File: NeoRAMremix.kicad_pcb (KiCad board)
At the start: 2 copper layers, 58.2 x 84.1 mm, 28 parts, among them P1 C64-Exp-Port, Q1 2N3904, SW1 Reset, U1 HM628512BFP-5, U2 HM628512BFP-5, U3 HM628512BFP-5, U4 HM628512BFP-5

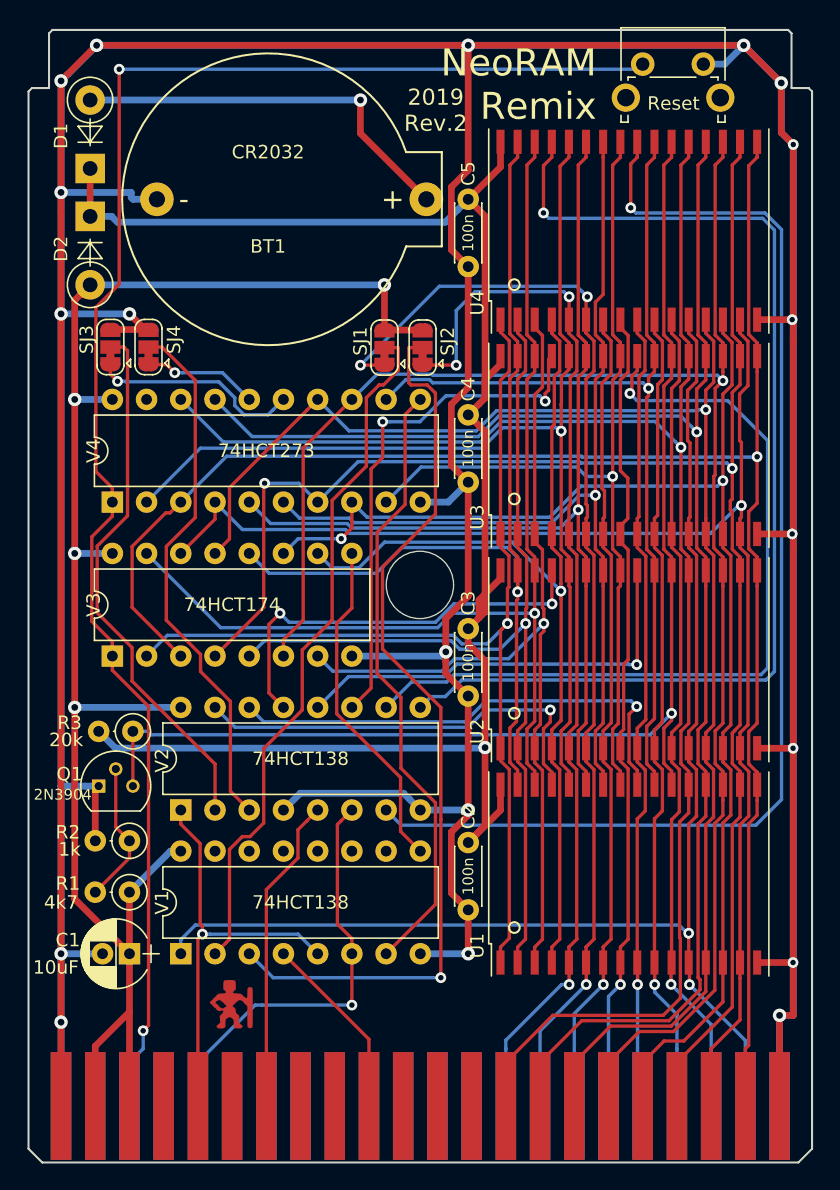
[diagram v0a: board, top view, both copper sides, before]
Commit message: Added JP1 to disable battery circuit for /CS.
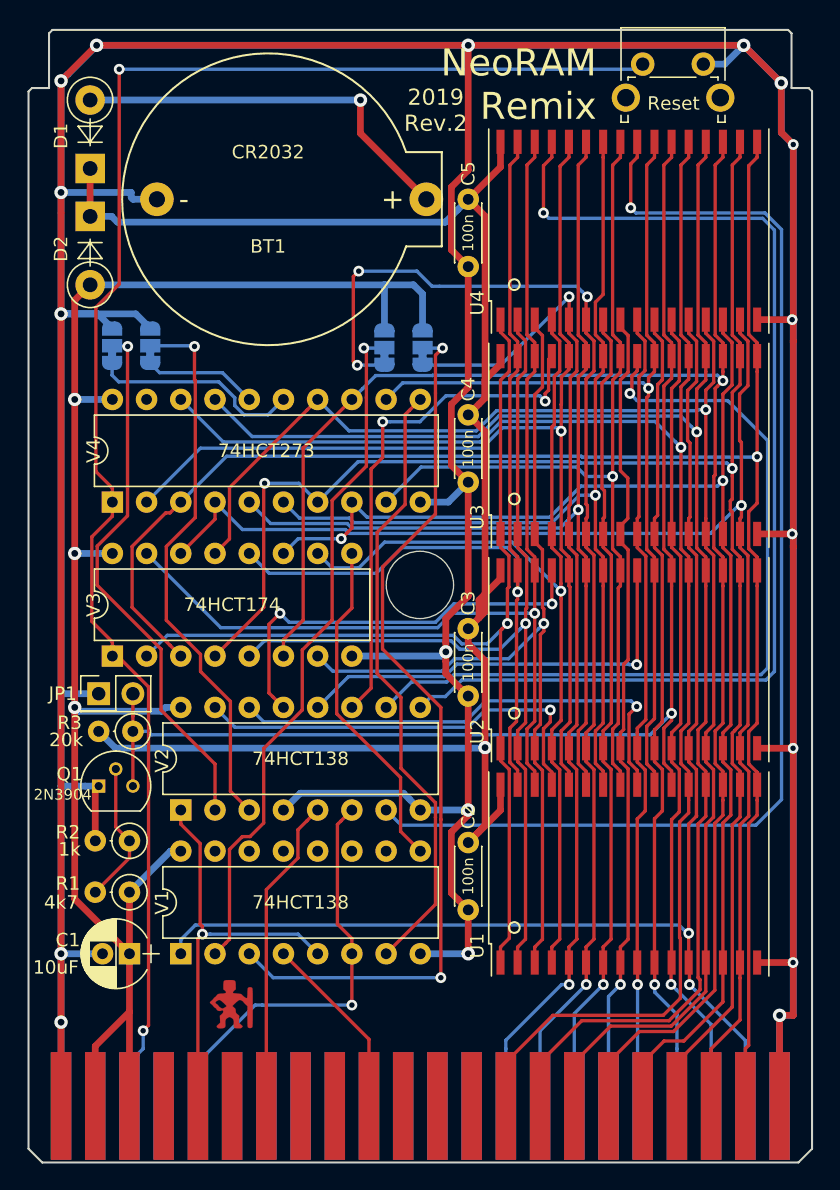
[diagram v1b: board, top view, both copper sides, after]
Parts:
- added JP1: no_battery, Pin_Headers:Pin_Header_Straight_2x01_Pitch2.54mm, F.Cu at (89.2, 100.1)
- SJ1, SJ2, SJ3, SJ4: moved to B.Cu
- moved SJ4 0.16 mm to (93.0, 74.2)
- moved SJ3 0.16 mm to (90.2, 74.2)
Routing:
- net /A6: track 84.5 -> 90.1 mm, vias 3 -> 4
- net GND: track 562.0 -> 566.3 mm, vias 19 -> 18
- net +5V: track 122.3 -> 125.5 mm, vias 4 -> 3
- net Net-(JP1-Pad2): track 94.0 -> 96.8 mm
- net /A7: track 79.5 -> 76.8 mm, vias 3 -> 2
- net Net-(SJ4-Pad2): track 39.8 -> 41.2 mm, vias 0 -> 1
- net Net-(SJ2-Pad2): track 67.7 -> 66.8 mm, vias 1 -> 2
- net Net-(SJ1-Pad2): track 52.2 -> 51.6 mm, vias 0 -> 1
- net Net-(SJ3-Pad2): track 40.0 -> 40.2 mm, vias 0 -> 1
- net Net-(SJ4-Pad1): track 8.55 -> 8.46 mm, vias 1 -> 0
- net Net-(SJ3-Pad1): vias 1 -> 0
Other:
- board text added: "NeoRAM Remix Rev.2 Original design (2007): http://www.x1541.de/ Remix (2019): https://www.hackup.net/"
- board text removed: "NeoRAM Remix Rev.1 Original design (2007): http://www.x1541.de/ Remix (2019): https://www.hackup.net/"

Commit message: Added repo URL.
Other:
- board text added: "NeoRAM Remix Rev.2 https://github.com/hackup/NeoRAMremix Original design (2007): http://www.x1541.de/ Remix (2019): https://www.hackup.net/"
- board text removed: "NeoRAM Remix Rev.2 Original design (2007): http://www.x1541.de/ Remix (2019): https://www.hackup.net/"
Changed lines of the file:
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@@
     )
   )
-  (gr_text "NeoRAM Remix Rev.2\nOriginal design (2007): http://www.x1541.de/\nRemix (2019): https://www.hackup.net/" (at 134.62 120.523 270) (layer B.SilkS)
+  (gr_text "NeoRAM Remix Rev.2\nhttps://github.com/hackup/NeoRAMremix\nOriginal design (2007): http://www.x1541.de/\nRemix (2019): https://www.hackup.net/" (at 134.62 120.523 270) (layer B.SilkS)
     (effects (font (size 1.5 1.5) (thickness 0.3)) (justify left mirror))
   )
@@
   (segment (start 91.44 112.268) (end 91.44 110.998) (width 0.25) (layer F.Cu) (net 26))
   (segment (start 88.9 114.808) (end 91.44 112.268) (width 0.25) (layer F.Cu) (net 26))
-  (segment (start 91.694 106.934) (end 91.694 102.87) (width 0.25) (layer F.Cu) (net 54))
-  (segment (start 131.683001 92.074999) (end 131.683001 90.924999) (width 0.25) (layer F.Cu) (net 54))
-  (segment (start 131.108 102.6297) (end 131.683001 102.054699) (width 0.25) (layer F.Cu) (net 54))
-  (segment (start 131.108 105.245) (end 131.108 102.6297) (width 0.25) (layer F.Cu) (net 54))
-  (segment (start 131.683001 105.820001) (end 131.108 105.245) (width 0.25) (layer F.Cu) (net 54))
-  (segment (start 131.683001 106.832999) (end 131.683001 105.820001) (width 0.25) (layer F.Cu) (net 54))
-  (segment (start 131.683001 76.654699) (end 131.683001 76.166999) (width 0.25) (layer F.Cu) (net 54))
-  (segment (start 131.683001 76.166999) (end 131.683001 75.016999) (width 0.25) (layer F.Cu) (net 54))
-  (segment (start 131.683001 89.934297) (end 131.108 89.359296) (width 0.25) (layer F.Cu) (net 54))
-  (segment (start 131.683001 90.924999) (end 131.683001 89.934297) (width 0.25) (layer F.Cu) (net 54))
-  (segment (start 131.108 77.2297) (end 131.683001 76.654699) (width 0.25) (layer F.Cu) (net 54))
-  (segment (start 131.108 89.359296) (end 131.108 77.2297) (width 0.25) (layer F.Cu) (net 54))
-  (segment (start 131.108 60.834) (end 131.683001 60.258999) (width 0.25) (layer F.Cu) (net 54))
-  (segment (start 131.683001 60.258999) (end 131.683001 59.108999) (width 0.25) (layer F.Cu) (net 54))
-  (segment (start 131.108 73.451296) (end 131.108 60.834) (width 0.25) (layer F.Cu) (net 54))
-  (segment (start 131.683001 75.016999) (end 131.683001 74.026297) (width 0.25) (layer F.Cu) (net 54))
-  (segment (start 131.683001 74.026297) (end 131.108 73.451296) (width 0.25) (layer F.Cu) (net 54))
-  (segment (start 92.82537 102.87) (end 93.07937 103.124) (width 0.25) (layer B.Cu) (net 54))
-  (segment (start 91.694 102.87) (end 92.82537 102.87) (width 0.25) (layer B.Cu) (net 54))
-  (via (at 131.683001 101.5365) (size 0.8) (drill 0.4) (layers F.Cu B.Cu) (net 54))
-  (segment (start 130.095501 103.124) (end 131.683001 101.5365) (width 0.25) (layer B.Cu) (net 54))
-  (segment (start 93.07937 103.124) (end 130.095501 103.124) (width 0.25) (layer B.Cu) (net 54))
-  (segment (start 131.683001 101.5365) (end 131.683001 92.074999) (width 0.25) (layer F.Cu) (net 54))
-  (segment (start 131.683001 102.054699) (end 131.683001 101.5365) (width 0.25) (layer F.Cu) (net 54))
   (segment (start 90.150005 76.434005) (end 90.150005 75.547036) (width 0.25) (layer B.Cu) (net 27))
   (segment (start 90.63827 76.92227) (end 90.150005 76.434005) (width 0.25) (layer B.Cu) (net 27))
@@
   (segment (start 96.266 76.755959) (end 96.325001 76.81496) (width 0.25) (layer F.Cu) (net 53))
   (segment (start 96.266 74.295) (end 96.266 76.755959) (width 0.25) (layer F.Cu) (net 53))
+  (segment (start 91.694 106.934) (end 91.694 102.87) (width 0.25) (layer F.Cu) (net 54))
+  (segment (start 131.683001 92.074999) (end 131.683001 90.924999) (width 0.25) (layer F.Cu) (net 54))
+  (segment (start 131.108 102.6297) (end 131.683001 102.054699) (width 0.25) (layer F.Cu) (net 54))
+  (segment (start 131.108 105.245) (end 131.108 102.6297) (width 0.25) (layer F.Cu) (net 54))
+  (segment (start 131.683001 105.820001) (end 131.108 105.245) (width 0.25) (layer F.Cu) (net 54))
+  (segment (start 131.683001 106.832999) (end 131.683001 105.820001) (width 0.25) (layer F.Cu) (net 54))
+  (segment (start 131.683001 76.654699) (end 131.683001 76.166999) (width 0.25) (layer F.Cu) (net 54))
+  (segment (start 131.683001 76.166999) (end 131.683001 75.016999) (width 0.25) (layer F.Cu) (net 54))
+  (segment (start 131.683001 89.934297) (end 131.108 89.359296) (width 0.25) (layer F.Cu) (net 54))
+  (segment (start 131.683001 90.924999) (end 131.683001 89.934297) (width 0.25) (layer F.Cu) (net 54))
+  (segment (start 131.108 77.2297) (end 131.683001 76.654699) (width 0.25) (layer F.Cu) (net 54))
+  (segment (start 131.108 89.359296) (end 131.108 77.2297) (width 0.25) (layer F.Cu) (net 54))
+  (segment (start 131.108 60.834) (end 131.683001 60.258999) (width 0.25) (layer F.Cu) (net 54))
+  (segment (start 131.683001 60.258999) (end 131.683001 59.108999) (width 0.25) (layer F.Cu) (net 54))
+  (segment (start 131.108 73.451296) (end 131.108 60.834) (width 0.25) (layer F.Cu) (net 54))
+  (segment (start 131.683001 75.016999) (end 131.683001 74.026297) (width 0.25) (layer F.Cu) (net 54))
+  (segment (start 131.683001 74.026297) (end 131.108 73.451296) (width 0.25) (layer F.Cu) (net 54))
+  (segment (start 92.82537 102.87) (end 93.07937 103.124) (width 0.25) (layer B.Cu) (net 54))
+  (segment (start 91.694 102.87) (end 92.82537 102.87) (width 0.25) (layer B.Cu) (net 54))
+  (via (at 131.683001 101.5365) (size 0.8) (drill 0.4) (layers F.Cu B.Cu) (net 54))
+  (segment (start 130.095501 103.124) (end 131.683001 101.5365) (width 0.25) (layer B.Cu) (net 54))
+  (segment (start 93.07937 103.124) (end 130.095501 103.124) (width 0.25) (layer B.Cu) (net 54))
+  (segment (start 131.683001 101.5365) (end 131.683001 92.074999) (width 0.25) (layer F.Cu) (net 54))
+  (segment (start 131.683001 102.054699) (end 131.683001 101.5365) (width 0.25) (layer F.Cu) (net 54))
   (segment (start 91.694 101.73863) (end 91.694 100.076) (width 0.25) (layer F.Cu) (net 54))
   (segment (start 91.694 102.87) (end 91.694 101.73863) (width 0.25) (layer F.Cu) (net 54))

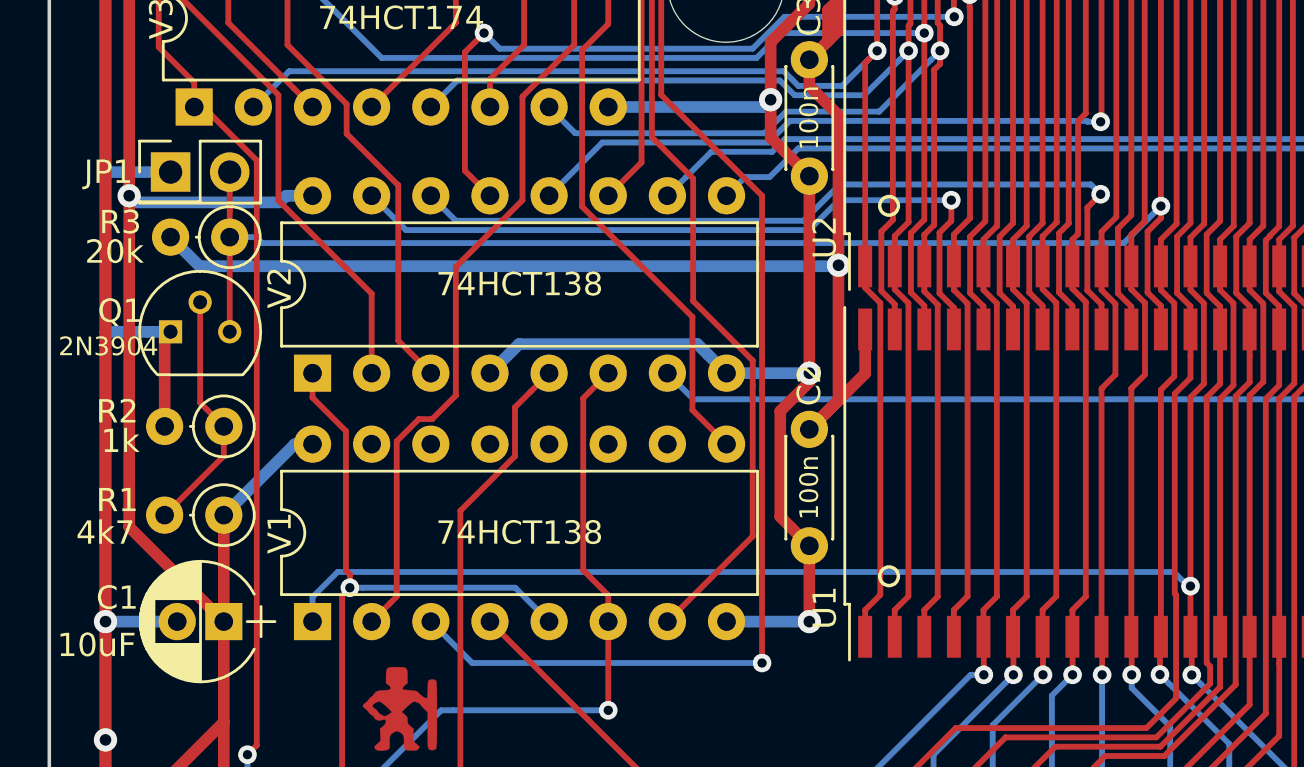
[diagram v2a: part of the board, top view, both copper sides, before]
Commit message: More room for JP1.
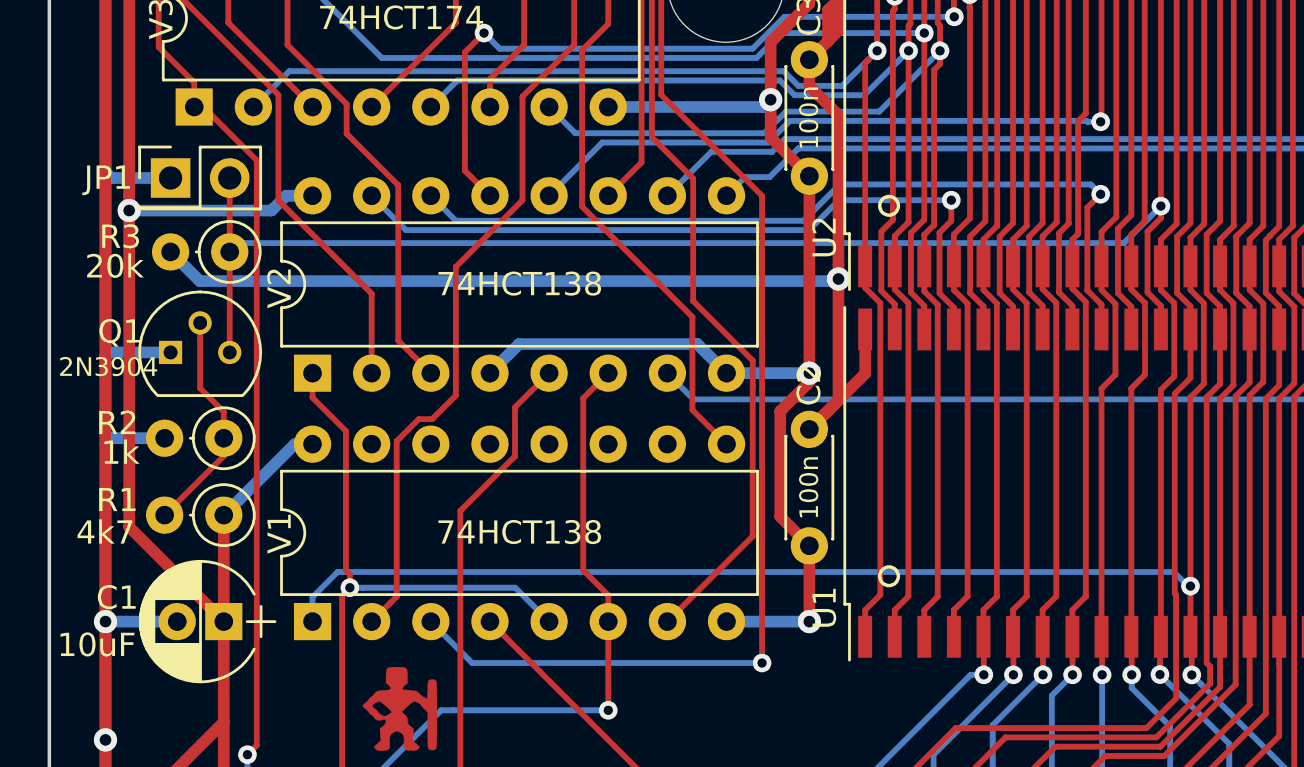
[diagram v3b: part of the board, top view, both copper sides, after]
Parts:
- moved Q1 0.89 mm to (89.2, 107.8)
- moved R3 0.63 mm to (91.7, 103.5)
- moved R2 0.51 mm to (91.4, 111.5)
- moved JP1 0.25 mm to (89.2, 100.3)
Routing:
- net GND: track 566.3 -> 564.9 mm
- net Net-(JP1-Pad2): track 96.8 -> 97.5 mm

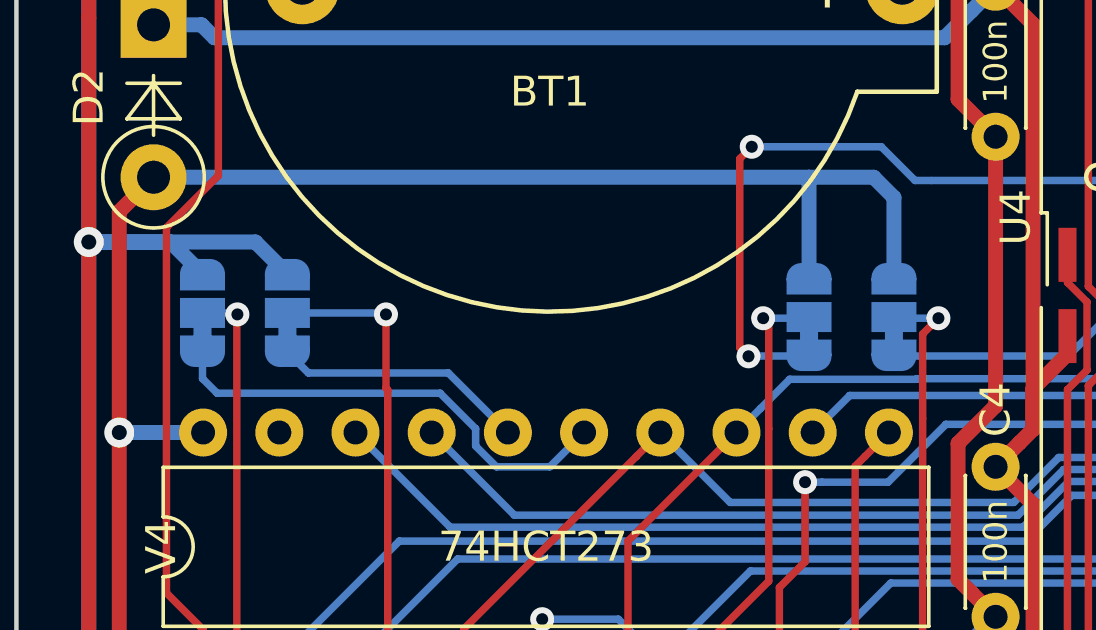
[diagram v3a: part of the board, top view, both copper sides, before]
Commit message: Improved solder jumper footprint.
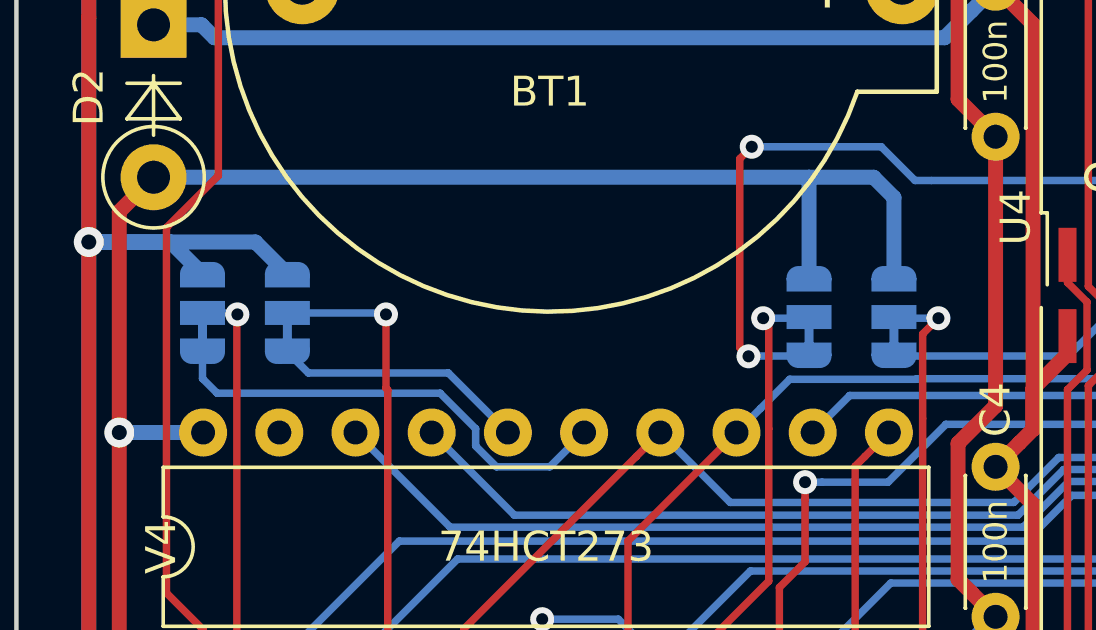
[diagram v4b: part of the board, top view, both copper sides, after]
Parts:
- SJ1, SJ2, SJ3, SJ4: footprint Jumper:SolderJumper-3_P1.3mm_Bridged12_RoundedPad1.0x1.5mm -> NeoRAMremix:SolderJumper-3_P1.3mm_Bridged12
